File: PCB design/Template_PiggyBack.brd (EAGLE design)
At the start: 63.5 x 88.6 mm, 46 parts, among them CN1 USB power supply, IC1 MCP6002, IC3 MCP6002, IC4 REG1117

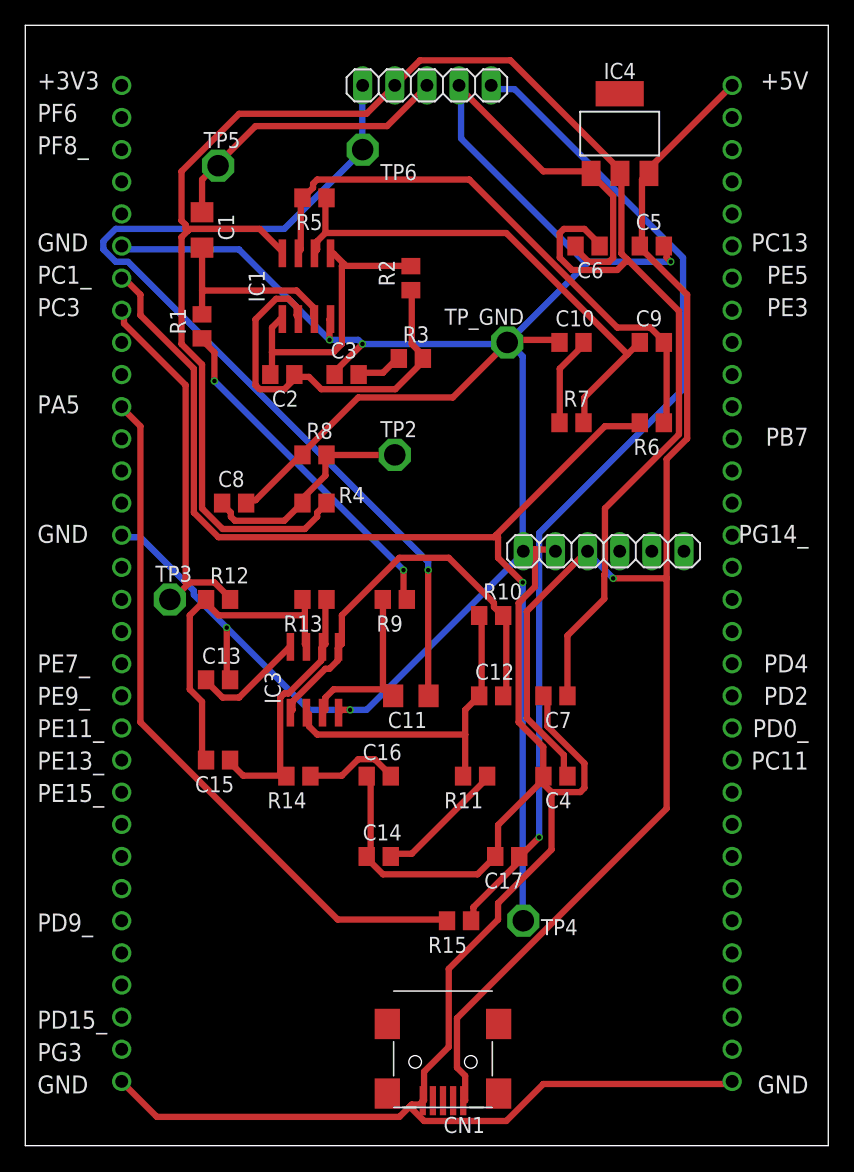
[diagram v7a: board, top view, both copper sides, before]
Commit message: adapted layout according to Rennhard's feedback
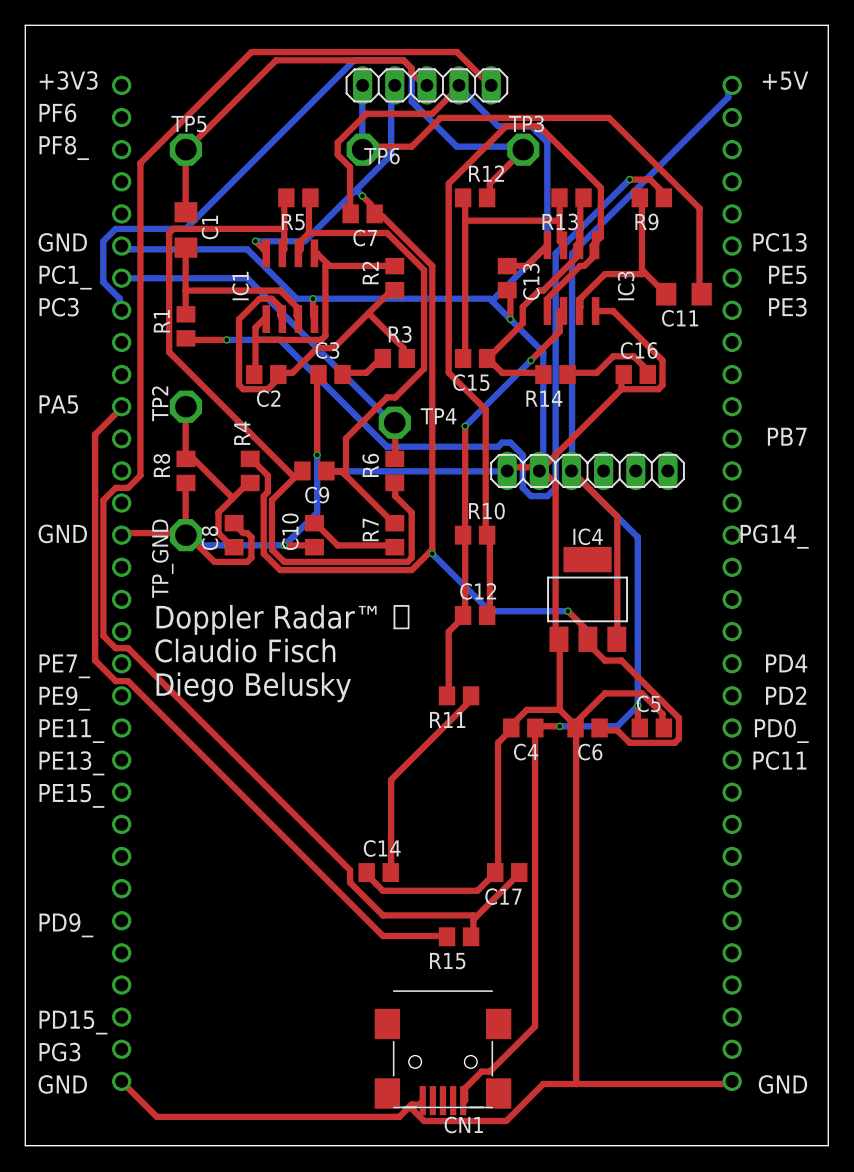
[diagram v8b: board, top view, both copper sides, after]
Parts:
- C4: value 1u -> 100n
- moved TP3 45.2 mm to (39.4, 78.7)
- moved C7 41.0 mm to (26.7, 73.7)
- moved TP4 40.7 mm to (29.2, 57.1), turned to 90 degrees
- moved C13 39.1 mm to (38.1, 68.6), turned to 270 degrees
- moved C11 38.4 mm to (52.1, 67.3)
- moved C5 38.1 mm to (49.5, 33.0)
- moved C6 38.1 mm to (44.5, 33.0)
- moved R12 37.7 mm to (35.6, 74.9)
- moved R13 37.7 mm to (43.2, 74.9)
- moved R9 37.7 mm to (49.5, 74.9)
- moved C16 37.7 mm to (48.3, 61.0)
- moved IC3 37.7 mm to (43.2, 68.6)
- moved R14 37.7 mm to (41.9, 61.0)
- moved C15 37.7 mm to (35.6, 62.2)
- moved IC4 36.9 mm to (44.5, 43.2)
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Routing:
- net PC1_: track 92.2 -> 29.2 mm, vias 1 -> 0
- net +3V3: track 148.9 -> 109.2 mm, vias 0 -> 4
- net V_GND: track 27.5 -> 67.0 mm
- net VCO: track 80.6 -> 117.5 mm, vias 1 -> 0
- net IF_Q: track 75.8 -> 42.5 mm, vias 1 -> 0
- net N$12: track 32.8 -> 63.4 mm
- net PC3: track 29.9 -> 54.7 mm
- net GND: track 336.4 -> 316.7 mm, vias 5 -> 4
- net N$7: track 45.9 -> 62.5 mm
- net N$9: track 27.2 -> 34.6 mm, vias 0 -> 2
- net +5V: track 121.5 -> 114.2 mm, vias 1 -> 2
- net N$15: track 10.4 -> 16.8 mm
- net VCC: track 8.95 -> 3.85 mm
- net IF_I: track 23.5 -> 27.9 mm
- net N$13: track 26.2 -> 24.2 mm
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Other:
- board text added: "Doppler Radar™ 📡 Claudio Fisch Diego Belusky"
